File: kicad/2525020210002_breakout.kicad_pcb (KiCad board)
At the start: 2 copper layers, 40 x 30 mm, 15 parts, among them J1 I2C_IN, J2 I2C_OUT, J3 Conn_01x04_Socket, U1 2525020210002

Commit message: README.md update, schematic m.hole sz lbl
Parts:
- H1, H2, H3, H4: value MountingHole -> MountingHole M3
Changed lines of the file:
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@@
     (descr "Capacitor SMD 0603 (1608 Metric), square (rectangular) end terminal, IPC_7351 nominal, (Body size source: IPC-SM-782 page 76, https://www.pcb-3d.com/wordpress/wp-content/uploads/ipc-sm-782a_amendment_1_and_2.pdf), generated with kicad-footprint-generator")
     (tags "capacitor")
-    (property "Sheetfile" "BiltongBoardSensorExpansion.kicad_sch")
+    (property "Sheetfile" "2525020210002_breakout.kicad_sch")
     (property "Sheetname" "")
     (property "ki_description" "Unpolarized capacitor")
@@
     (descr "Mounting Hole 3.2mm, no annular, M3")
     (tags "mounting hole 3.2mm no annular m3")
-    (property "Sheetfile" "BiltongBoardSensorExpansion.kicad_sch")
+    (property "Sheetfile" "2525020210002_breakout.kicad_sch")
     (property "Sheetname" "")
     (property "ki_description" "Mounting Hole without connection")
@@
         (effects (font (size 1 1) (thickness 0.15)))
     )
-    (fp_text value "MountingHole" (at 0 4.2) (layer "F.Fab")
+    (fp_text value "MountingHole M3" (at 0 4.2) (layer "F.Fab")
         (effects (font (size 1 1) (thickness 0.15)))
     )
@@
     (descr "Resistor SMD 0603 (1608 Metric), square (rectangular) end terminal, IPC_7351 nominal, (Body size source: IPC-SM-782 page 72, https://www.pcb-3d.com/wordpress/wp-content/uploads/ipc-sm-782a_amendment_1_and_2.pdf), generated with kicad-footprint-generator")
     (tags "resistor")
-    (property "Sheetfile" "BiltongBoardSensorExpansion.kicad_sch")
+    (property "Sheetfile" "2525020210002_breakout.kicad_sch")
     (property "Sheetname" "")
     (property "ki_description" "Resistor")
@@
     (descr "Resistor SMD 0603 (1608 Metric), square (rectangular) end terminal, IPC_7351 nominal, (Body size source: IPC-SM-782 page 72, https://www.pcb-3d.com/wordpress/wp-content/uploads/ipc-sm-782a_amendment_1_and_2.pdf), generated with kicad-footprint-generator")
     (tags "resistor")
-    (property "Sheetfile" "BiltongBoardSensorExpansion.kicad_sch")
+    (property "Sheetfile" "2525020210002_breakout.kicad_sch")
     (property "Sheetname" "")
     (property "ki_description" "Resistor")
@@
     (descr "JST PH series connector, B4B-PH-K (http://www.jst-mfg.com/product/pdf/eng/ePH.pdf), generated with kicad-footprint-generator")
     (tags "connector JST PH side entry")
-    (property "Sheetfile" "BiltongBoardSensorExpansion.kicad_sch")
+    (property "Sheetfile" "2525020210002_breakout.kicad_sch")
     (property "Sheetname" "")
     (property "ki_description" "Generic connector, single row, 01x04, script generated (kicad-library-utils/schlib/autogen/connector/)")
@@
     (descr "Through hole straight pin header, 1x04, 2.54mm pitch, single row")
     (tags "Through hole pin header THT 1x04 2.54mm single row")
-    (property "Sheetfile" "BiltongBoardSensorExpansion.kicad_sch")
+    (property "Sheetfile" "2525020210002_breakout.kicad_sch")
     (property "Sheetname" "")
     (property "ki_description" "Generic connector, single row, 01x04, script generated")
@@
     (property "Mouser Part Number" "710-2525020210002")
     (property "Mouser Price/Stock" "https://www.mouser.co.uk/ProductDetail/Wurth-Elektronik/2525020210002?qs=HoCaDK9Nz5fMHXWEMIcK9w%3D%3D")
-    (property "Sheetfile" "BiltongBoardSensorExpansion.kicad_sch")
+    (property "Sheetfile" "2525020210002_breakout.kicad_sch")
     (property "Sheetname" "")
     (property "ki_description" "Board Mount Humidity Sensors WSEN-HIDS Humidity sensor 3% Accuracy 0 to 100% RH")
@@
     (descr "Resistor SMD 0603 (1608 Metric), square (rectangular) end terminal, IPC_7351 nominal, (Body size source: IPC-SM-782 page 72, https://www.pcb-3d.com/wordpress/wp-content/uploads/ipc-sm-782a_amendment_1_and_2.pdf), generated with kicad-footprint-generator")
     (tags "resistor")
-    (property "Sheetfile" "BiltongBoardSensorExpansion.kicad_sch")
+    (property "Sheetfile" "2525020210002_breakout.kicad_sch")
     (property "Sheetname" "")
     (property "ki_description" "Resistor")
@@
     (descr "Mounting Hole 3.2mm, no annular, M3")
     (tags "mounting hole 3.2mm no annular m3")
-    (property "Sheetfile" "BiltongBoardSensorExpansion.kicad_sch")
+    (property "Sheetfile" "2525020210002_breakout.kicad_sch")
     (property "Sheetname" "")
     (property "ki_description" "Mounting Hole without connection")
@@
         (effects (font (size 1 1) (thickness 0.15)))
     )
-    (fp_text value "MountingHole" (at 0 4.2) (layer "F.Fab")
+    (fp_text value "MountingHole M3" (at 0 4.2) (layer "F.Fab")
         (effects (font (size 1 1) (thickness 0.15)))
     )
@@
     (descr "Mounting Hole 3.2mm, no annular, M3")
     (tags "mounting hole 3.2mm no annular m3")
-    (property "Sheetfile" "BiltongBoardSensorExpansion.kicad_sch")
+    (property "Sheetfile" "2525020210002_breakout.kicad_sch")
     (property "Sheetname" "")
     (property "ki_description" "Mounting Hole without connection")
@@
         (effects (font (size 1 1) (thickness 0.15)))
     )
-    (fp_text value "MountingHole" (at 0 4.2) (layer "F.Fab")
+    (fp_text value "MountingHole M3" (at 0 4.2) (layer "F.Fab")
         (effects (font (size 1 1) (thickness 0.15)))
     )
@@
     (descr "LED SMD 0603 (1608 Metric), square (rectangular) end terminal, IPC_7351 nominal, (Body size source: http://www.tortai-tech.com/upload/download/2011102023233369053.pdf), generated with kicad-footprint-generator")
     (tags "LED")
-    (property "Sheetfile" "BiltongBoardSensorExpansion.kicad_sch")
+    (property "Sheetfile" "2525020210002_breakout.kicad_sch")
     (property "Sheetname" "")
     (property "ki_description" "Light emitting diode")
@@
     (descr "JST PH series connector, B4B-PH-K (http://www.jst-mfg.com/product/pdf/eng/ePH.pdf), generated with kicad-footprint-generator")
     (tags "connector JST PH side entry")
-    (property "Sheetfile" "BiltongBoardSensorExpansion.kicad_sch")
+    (property "Sheetfile" "2525020210002_breakout.kicad_sch")
     (property "Sheetname" "")
     (property "ki_description" "Generic connector, single row, 01x04, script generated (kicad-library-utils/schlib/autogen/connector/)")
@@
     (descr "Mounting Hole 3.2mm, no annular, M3")
     (tags "mounting hole 3.2mm no annular m3")
-    (property "Sheetfile" "BiltongBoardSensorExpansion.kicad_sch")
+    (property "Sheetfile" "2525020210002_breakout.kicad_sch")
     (property "Sheetname" "")
     (property "ki_description" "Mounting Hole without connection")
@@
         (effects (font (size 1 1) (thickness 0.15)))
     )
-    (fp_text value "MountingHole" (at -0.25 3.325) (layer "F.Fab")
-        (effects (font (size 1 1) (thickness 0.15)))
-    )
+    (fp_text value "MountingHole M3" (at -0.25 3.325) (layer "F.Fab")
+        (effects (font (size 1 1) (thickness 0.15)))
+    )

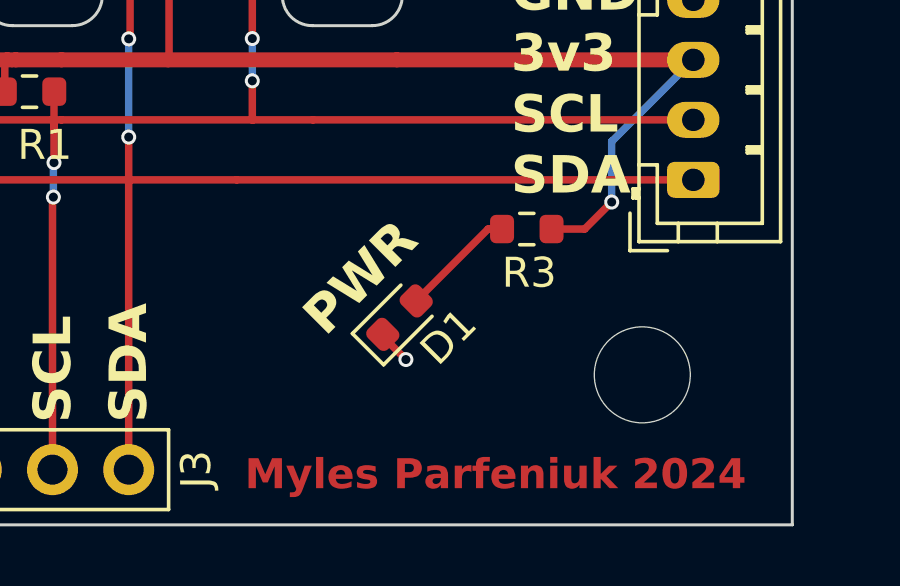
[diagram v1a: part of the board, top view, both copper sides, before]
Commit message: fxd exposed gnd, add r.ss lbls, PCBWay sponsorship
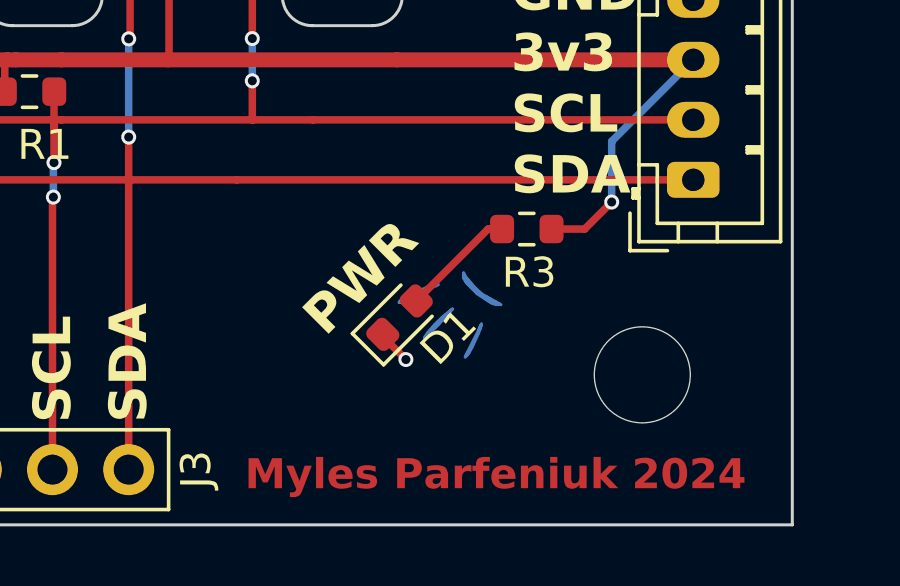
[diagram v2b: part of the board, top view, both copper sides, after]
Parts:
- added G***: LOGO, BiltongBoardSensorExpansion:pcbway_logo, B.Cu at (140.2, 88.8)
- added G***: LOGO, BiltongBoardSensorExpansion:sig_fc_10x11.5mm, B.Cu at (148.8, 102.1)
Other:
- board text added: "Powered by"

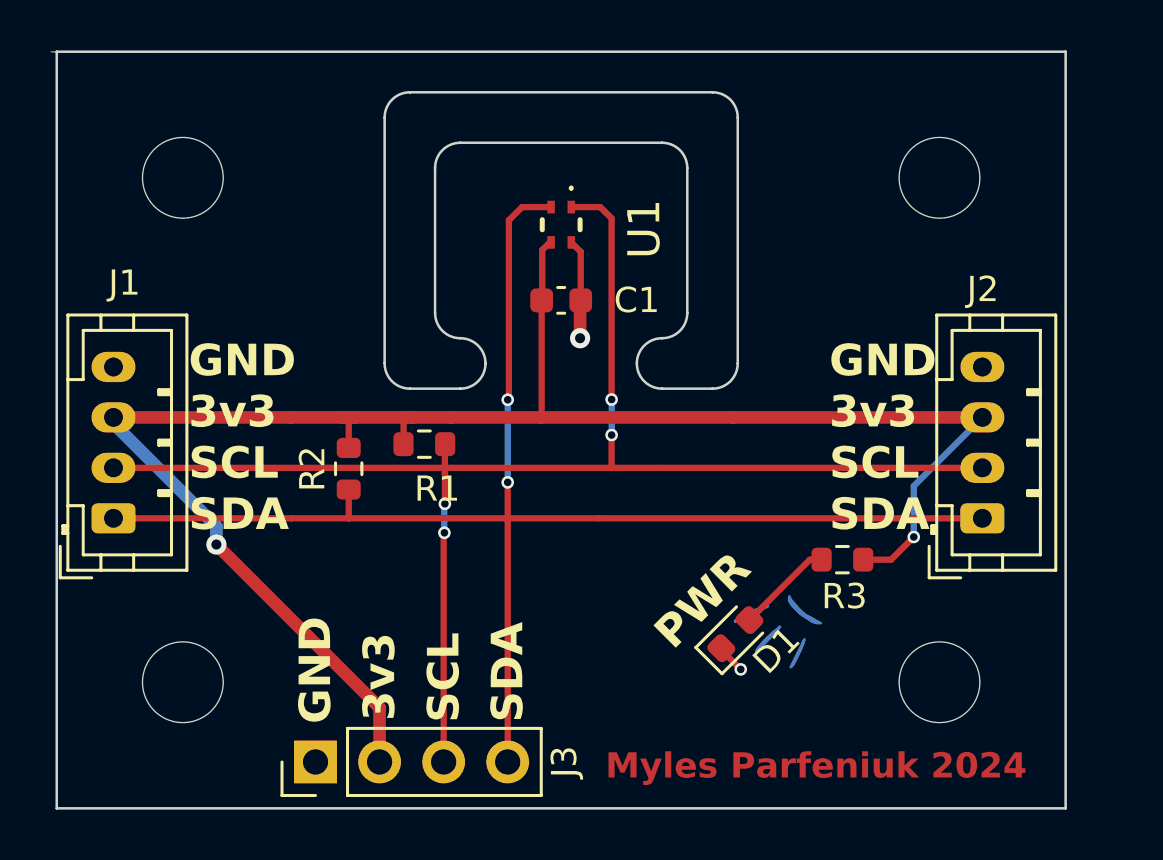
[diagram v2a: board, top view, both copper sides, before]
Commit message: fixed all DRC violations
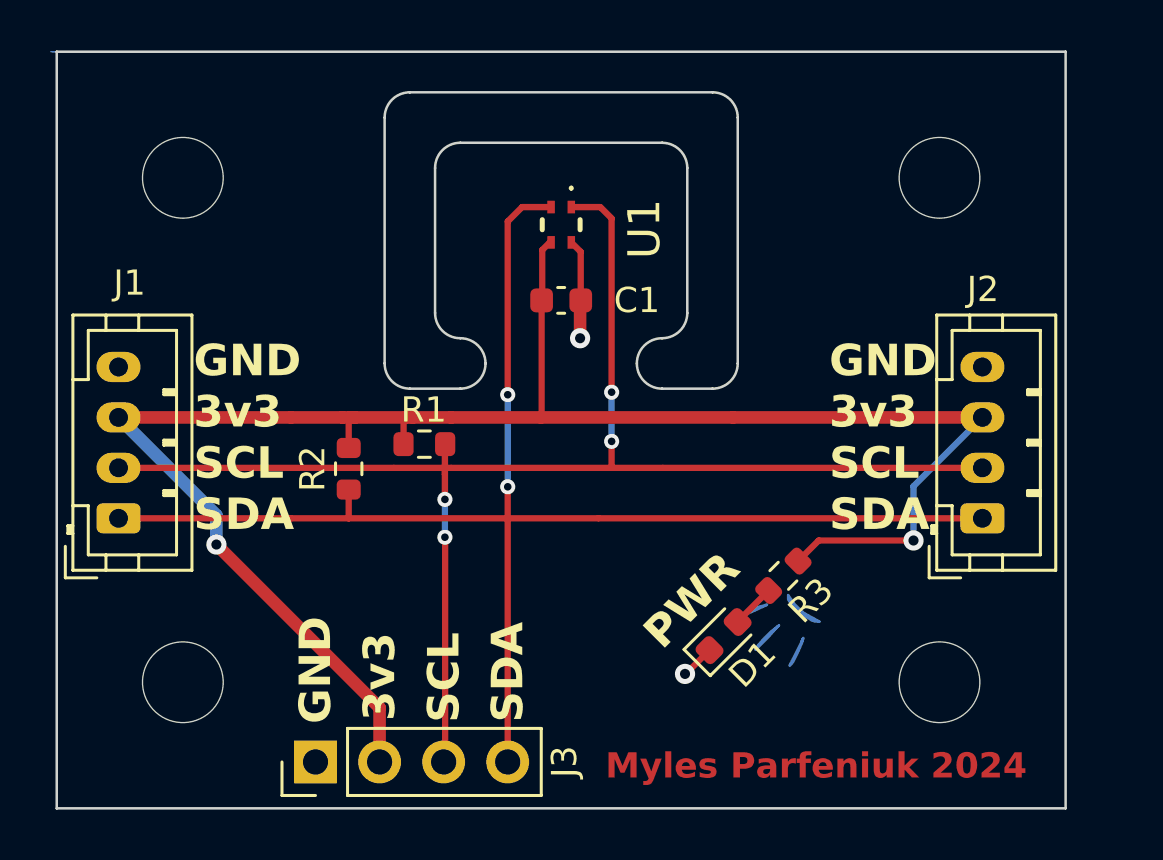
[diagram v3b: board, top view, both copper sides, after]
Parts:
- removed the G*** at (148.8, 102.1)
- added G***: LOGO, BiltongBoardSensorExpansion:sig_fc_screen_10x11.5mm, B.Cu at (148.8, 102.0)
- moved R3 2.43 mm to (149.1, 101.8), turned to 45 degrees
- moved D1 0.47 mm to (146.7, 104.2)
- moved J1 0.20 mm to (122.7, 99.5)
- moved G*** 0.16 mm to (140.3, 89.0)
- moved G*** 0.07 mm to (148.8, 102.0)
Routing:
- net +3V3: track 70.6 -> 73.0 mm
- net Net-(D1-A): track 3.85 -> 1.76 mm

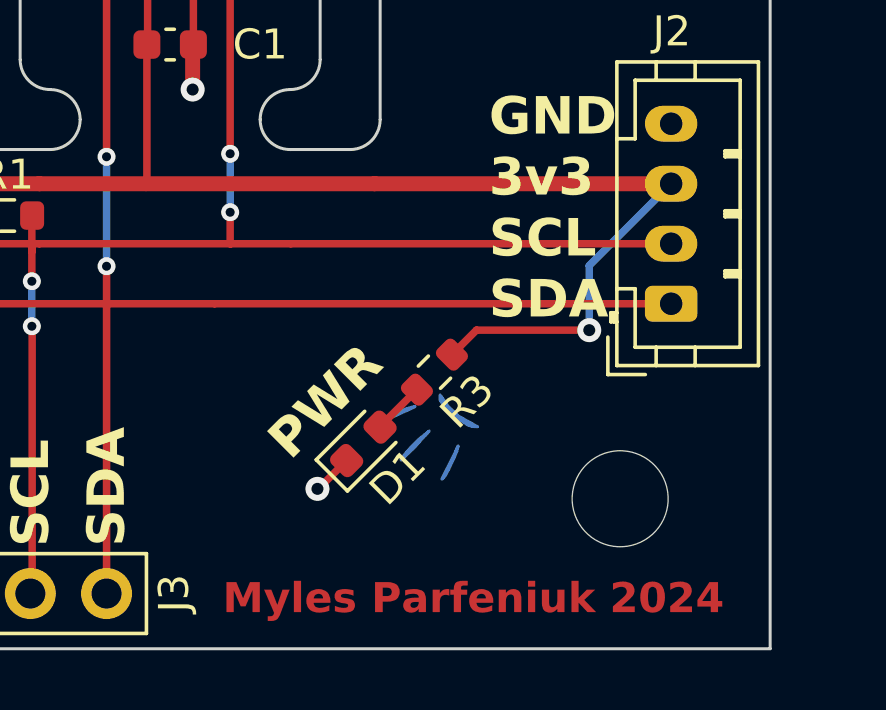
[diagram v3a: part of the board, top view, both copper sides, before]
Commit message: modified pwr diode trace
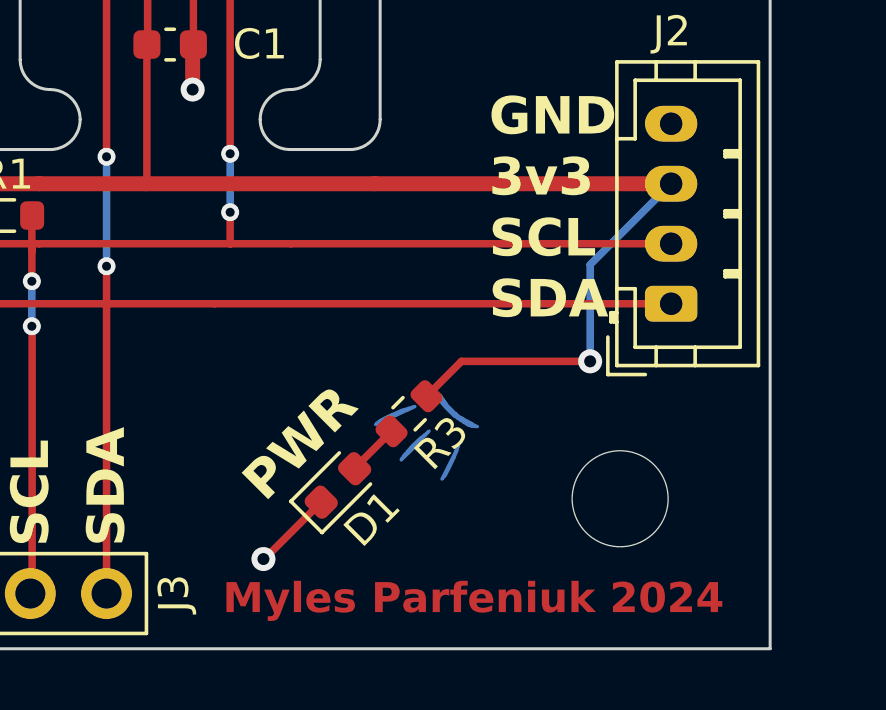
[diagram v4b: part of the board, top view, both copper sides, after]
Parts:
- moved R3 1.62 mm to (148.2, 103.2)
- moved D1 1.62 mm to (145.8, 105.6)
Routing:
- net +3V3: track 73.0 -> 75.0 mm
- net GND: track 5.33 -> 6.68 mm
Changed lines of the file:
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@@
   )
   (footprint "Resistor_SMD:R_0603_1608Metric" (layer "F.Cu")
-    (at 149.06 101.78 45)
+    (at 148.213363 103.166637 45)
     (descr "Resistor SMD 0603 (1608 Metric), square (rectangular) end terminal, IPC_7351 nominal, (Body size source: IPC-SM-782 page 72, https://www.pcb-3d.com/wordpress/wp-content/uploads/ipc-sm-782a_amendment_1_and_2.pdf), generated with kicad-footprint-generator")
     (tags "resistor")
@@
   )
   (footprint "LED_SMD:LED_0603_1608Metric" (layer "F.Cu")
-    (at 146.69 104.17 45)
+    (at 145.843363 105.556637 45)
     (descr "LED SMD 0603 (1608 Metric), square (rectangular) end terminal, IPC_7351 nominal, (Body size source: http://www.tortai-tech.com/upload/download/2011102023233369053.pdf), generated with kicad-footprint-generator")
     (tags "LED")
@@
   (gr_line (start 140.21 110.98) (end 140.21 80.98)
     (stroke (width 0.15) (type default)) (layer "User.2"))
-  (gr_line (start 146.68 104.18) (end 144.47 101.97)
+  (gr_line (start 145.833363 105.566637) (end 143.623363 103.356637)
     (stroke (width 0.15) (type default)) (layer "User.2"))
   (gr_line (start 160.25 91.45) (end 160.25 83.45)
@@
     (effects (font (size 1.25 1.25) (thickness 0.3) bold) (justify left bottom))
   )
-  (gr_text "PWR" (at 144.36 104.85 45) (layer "F.SilkS")
+  (gr_text "PWR" (at 143.513363 106.236637 45) (layer "F.SilkS")
     (effects (font (size 1.25 1.25) (thickness 0.3) bold) (justify left bottom))
   )
@@
   )
   (segment (start 129.54 95.5) (end 131.572 95.5) (width 0.5) (layer "F.Cu") (net 1))
+  (segment (start 149.96 101.42) (end 148.796726 102.583274) (width 0.25) (layer "F.Cu") (net 1))
   (segment (start 133.05 109.16) (end 133.05 107.01) (width 0.5) (layer "F.Cu") (net 1))
   (segment (start 134.08 95.5) (end 134.366 95.5) (width 0.5) (layer "F.Cu") (net 1))
@@
   (segment (start 139.446 95.5) (end 147.066 95.5) (width 0.5) (layer "F.Cu") (net 1))
   (segment (start 132.08 95.5) (end 134.08 95.5) (width 0.5) (layer "F.Cu") (net 1))
-  (segment (start 150.46 100.38) (end 149.643363 101.196637) (width 0.25) (layer "F.Cu") (net 1))
   (segment (start 131.954 95.626) (end 132.08 95.5) (width 0.25) (layer "F.Cu") (net 1))
   (segment (start 122.5 95.5) (end 129.54 95.5) (width 0.5) (layer "F.Cu") (net 1))
   (segment (start 139.5 88.86) (end 139.5 90.835) (width 0.25) (layer "F.Cu") (net 1))
   (segment (start 133.05 107.01) (end 126.58 100.54) (width 0.5) (layer "F.Cu") (net 1))
-  (segment (start 154.22 100.38) (end 150.46 100.38) (width 0.25) (layer "F.Cu") (net 1))
   (segment (start 139.475 90.86) (end 139.475 95.471) (width 0.25) (layer "F.Cu") (net 1))
   (segment (start 135.89 95.5) (end 139.446 95.5) (width 0.5) (layer "F.Cu") (net 1))
@@
   (segment (start 139.475 95.471) (end 139.446 95.5) (width 0.25) (layer "F.Cu") (net 1))
   (segment (start 131.572 95.5) (end 131.87 95.5) (width 0.5) (layer "F.Cu") (net 1))
+  (segment (start 154.25 101.42) (end 149.96 101.42) (width 0.25) (layer "F.Cu") (net 1))
   (segment (start 134.24 95.626) (end 134.366 95.5) (width 0.25) (layer "F.Cu") (net 1))
   (segment (start 131.826 96.711) (end 131.826 95.544) (width 0.25) (layer "F.Cu") (net 1))
@@
   (segment (start 131.826 95.544) (end 131.87 95.5) (width 0.25) (layer "F.Cu") (net 1))
   (via (at 126.58 100.54) (size 0.8) (drill 0.4) (layers "F.Cu" "B.Cu") (net 1))
-  (via (at 154.22 100.38) (size 0.8) (drill 0.4) (layers "F.Cu" "B.Cu") (net 1))
+  (via (at 154.25 101.42) (size 0.8) (drill 0.4) (layers "F.Cu" "B.Cu") (net 1))
   (segment (start 126.58 99.38) (end 122.7 95.5) (width 0.5) (layer "B.Cu") (net 1))
-  (segment (start 154.22 98.23) (end 156.95 95.5) (width 0.25) (layer "B.Cu") (net 1))
-  (segment (start 154.22 100.38) (end 154.22 98.23) (width 0.25) (layer "B.Cu") (net 1))
   (segment (start 126.58 100.54) (end 126.58 99.38) (width 0.5) (layer "B.Cu") (net 1))
+  (segment (start 154.25 101.42) (end 154.25 98.2) (width 0.25) (layer "B.Cu") (net 1))
+  (segment (start 154.25 98.2) (end 156.95 95.5) (width 0.25) (layer "B.Cu") (net 1))
+  (segment (start 143.36 108.01) (end 143.39 108.01) (width 0.25) (layer "F.Cu") (net 2))
   (segment (start 141 90.885) (end 141 92.36) (width 0.5) (layer "F.Cu") (net 2))
   (segment (start 141.025 88.935) (end 140.65 88.56) (width 0.25) (layer "F.Cu") (net 2))
   (segment (start 141.025 90.86) (end 141 90.885) (width 0.25) (layer "F.Cu") (net 2))
-  (segment (start 145.16 105.67) (end 145.19 105.67) (width 0.25) (layer "F.Cu") (net 2))
   (segment (start 141.025 90.86) (end 141.025 88.935) (width 0.25) (layer "F.Cu") (net 2))
-  (segment (start 145.19 105.67) (end 146.133153 104.726847) (width 0.25) (layer "F.Cu") (net 2))
+  (segment (start 143.39 108.01) (end 145.286516 106.113484) (width 0.25) (layer "F.Cu") (net 2))
   (via (at 141 92.36) (size 0.8) (drill 0.4) (layers "F.Cu" "B.Cu") (net 2))
-  (via (at 145.16 105.67) (size 0.8) (drill 0.4) (layers "F.Cu" "B.Cu") (net 2))
+  (via (at 143.36 108.01) (size 0.8) (drill 0.4) (layers "F.Cu" "B.Cu") (net 2))
   (segment (start 135.57 97.5) (end 133.604 97.5) (width 0.25) (layer "F.Cu") (net 3))
   (segment (start 142.24 97.5) (end 135.89 97.5) (width 0.25) (layer "F.Cu") (net 3))
@@
   (via (at 138.13 98.25) (size 0.6) (drill 0.3) (layers "F.Cu" "B.Cu") (net 4))
   (segment (start 138.13 94.62) (end 138.13 98.25) (width 0.25) (layer "B.Cu") (net 4))
-  (segment (start 147.246847 103.593153) (end 147.246847 103.613153) (width 0.25) (layer "F.Cu") (net 5))
-  (segment (start 148.476637 102.363363) (end 147.246847 103.593153) (width 0.25) (layer "F.Cu") (net 5))
+  (segment (start 147.63 103.75) (end 146.40021 104.97979) (width 0.25) (layer "F.Cu") (net 5))
   (zone (net 2) (net_name "GND") (layer "B.Cu") (hatch edge 0.5)
     (connect_pads (clearance 0.5))
